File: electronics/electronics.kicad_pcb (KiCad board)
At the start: 2 copper layers, 155.2 x 120 mm, 69 parts, among them J1 GND NetTie, J2 Conn_01x02, J3 Conn 12V Out 5ch, J4 Chargers_Conn, J5 12V_BusBar, J6 GND_Busbar, J7 Conn_01x02, J9 water_sensor_conn, U1 AZ1117-ADJ, U10 BTS7006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

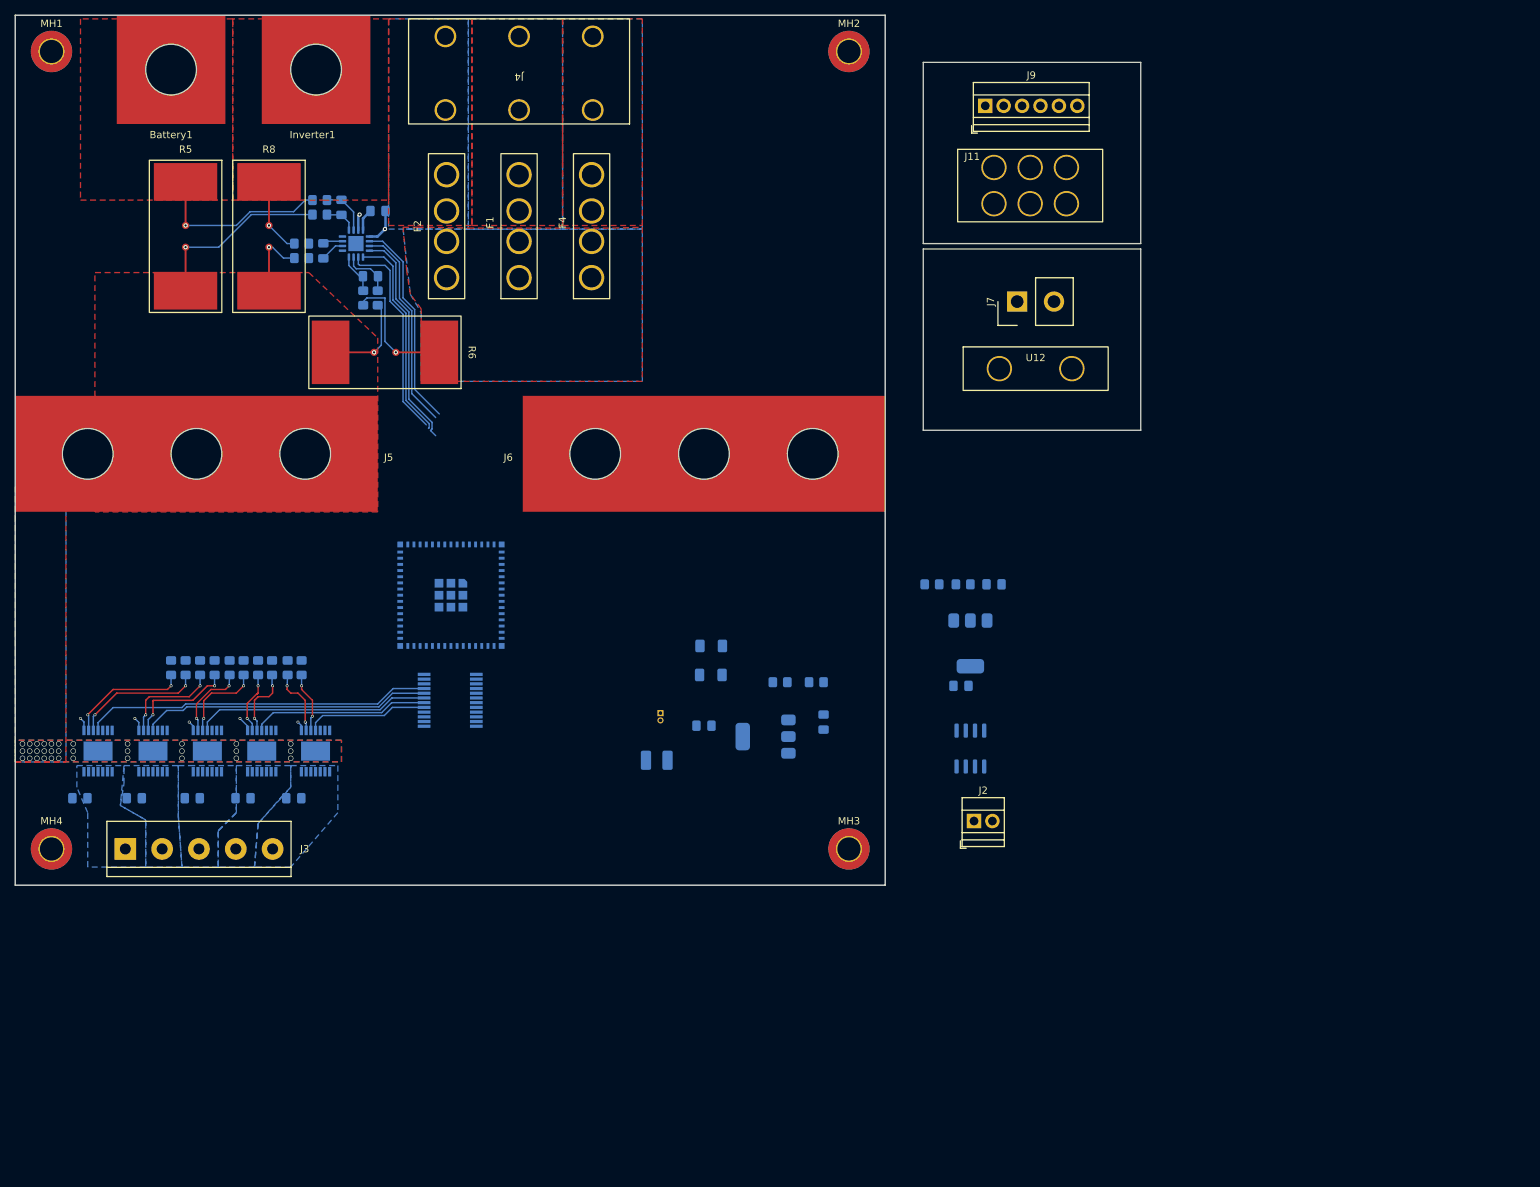
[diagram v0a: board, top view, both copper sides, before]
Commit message: big-55A-switch added
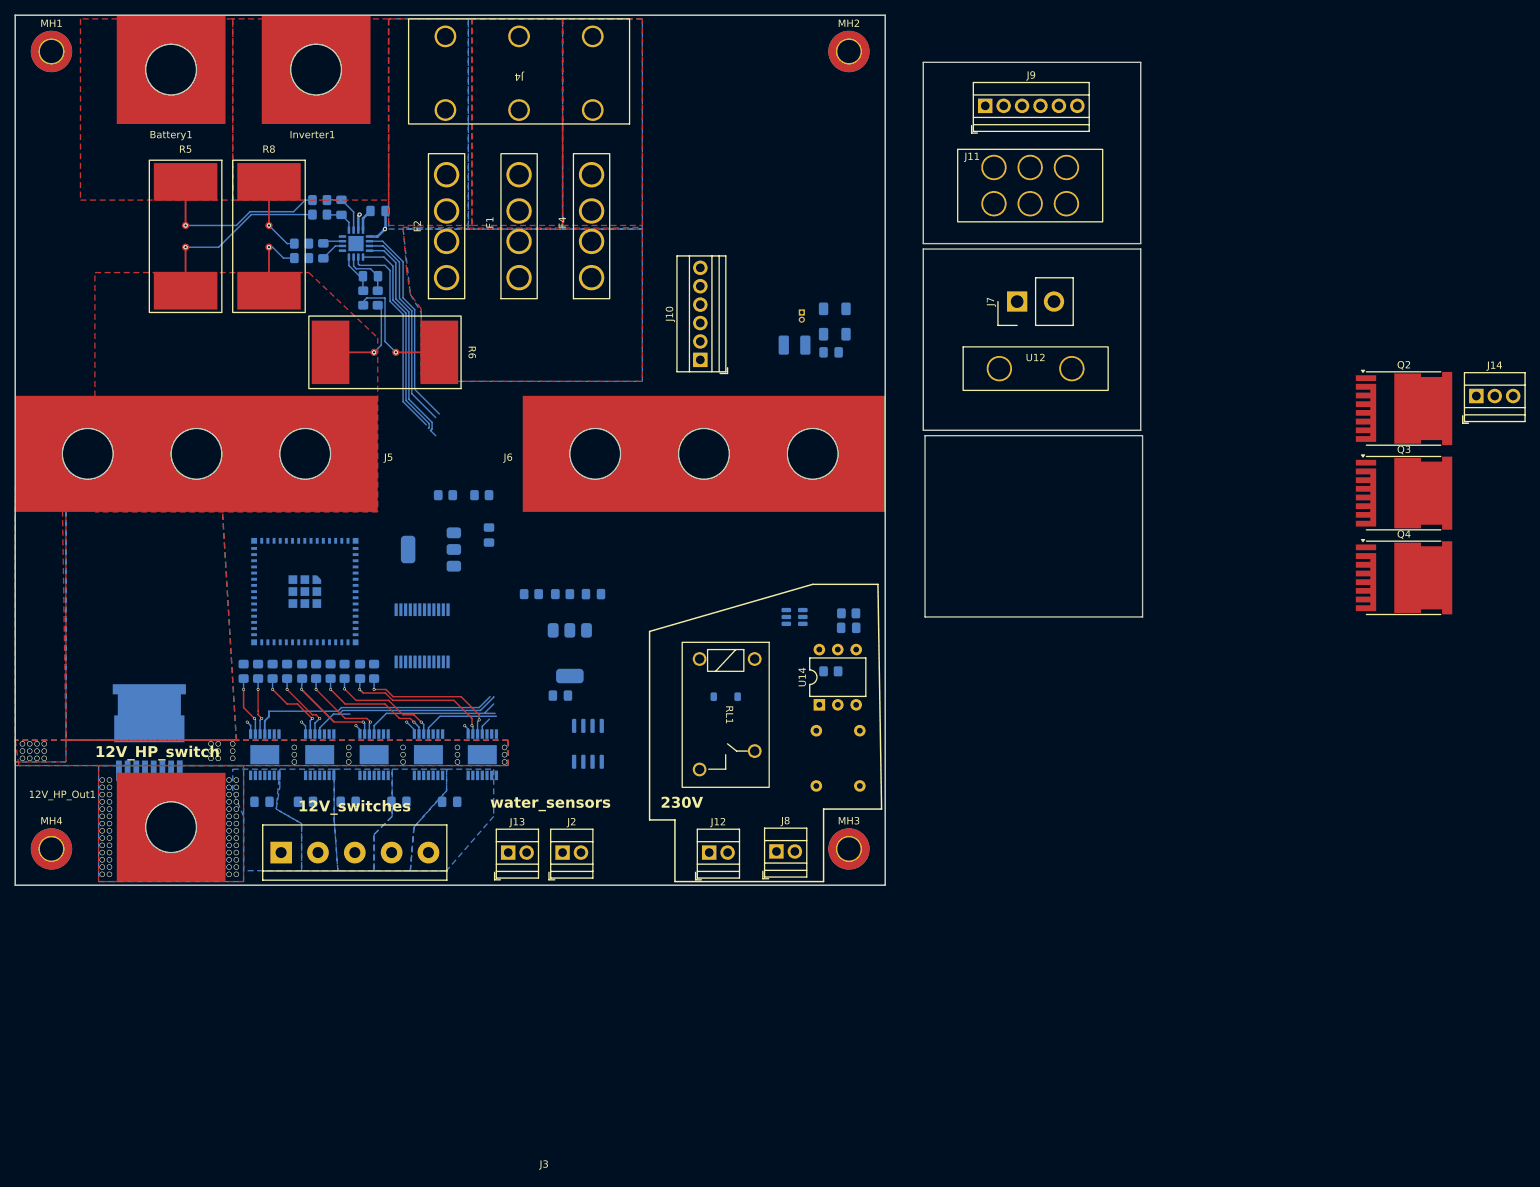
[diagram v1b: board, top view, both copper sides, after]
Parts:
- added 12V_HP_Out1: ~, HeavyDuty:high_current_pad, F.Cu at (41.5, 132.0)
- added C9: 4.7uF, Capacitor_SMD:C_0805_2012Metric_Pad1.18x1.45mm_HandSolder, B.Cu at (135.0, 104.5)
- added D2: 1N4148W, Diode_SMD:D_SOD-123, B.Cu at (118.0, 114.0)
- added J10: water_sensor_conn, TerminalBlock:TerminalBlock_Xinya_XY308-2.54-6P_1x06_P2.54mm_Horizontal, F.Cu at (114.5, 67.5)
- added J12: Conn_01x02, TerminalBlock:TerminalBlock_Xinya_XY308-2.54-2P_1x02_P2.54mm_Horizontal, F.Cu at (115.7, 135.5)
- added J13: grey_water_sensor, TerminalBlock:TerminalBlock_Xinya_XY308-2.54-2P_1x02_P2.54mm_Horizontal, F.Cu at (88.0, 135.5)
- added J14: Conn_01x03, TerminalBlock:TerminalBlock_Xinya_XY308-2.54-3P_1x03_P2.54mm_Horizontal, F.Cu at (221.5, 72.5)
- added J8: Conn_01x02, TerminalBlock:TerminalBlock_Xinya_XY308-2.54-2P_1x02_P2.54mm_Horizontal, F.Cu at (125.0, 135.3)
- added Q2: IRF6802SD, Package_TO_SOT_SMD:Infineon_PG-HSOF-8-1, F.Cu at (211.6, 74.2)
- added Q3: IRF6802SD, Package_TO_SOT_SMD:Infineon_PG-HSOF-8-1, F.Cu at (211.6, 85.9)
- added Q4: IRF6802SD, Package_TO_SOT_SMD:Infineon_PG-HSOF-8-1, F.Cu at (211.6, 97.6)
- added R17: 100k, Resistor_THT:R_Axial_DIN0207_L6.3mm_D2.5mm_P7.62mm_Horizontal, B.Cu at (130.5, 126.3)
- added R18: 100k, Resistor_THT:R_Axial_DIN0207_L6.3mm_D2.5mm_P7.62mm_Horizontal, B.Cu at (136.5, 126.3)
- added R19: 4.7kΩ, Resistor_SMD:R_0805_2012Metric_Pad1.20x1.40mm_HandSolder, B.Cu at (132.5, 110.5)
- added R20: 50 Ohm, Resistor_SMD:R_0805_2012Metric_Pad1.20x1.40mm_HandSolder, B.Cu at (135.0, 102.5)
- added RL1: AZSR131-1AE-12D, HeavyDuty:PRE29-same-sky, F.Cu at (119.0, 116.5)
- added U13: BTS50010, HeavyDuty:PG-HSOF-8, B.Cu at (38.0, 119.0)
- added U14: H11AA1, Package_DIP:DIP-6_W7.62mm, F.Cu at (130.9, 115.1)
- added U15: CNY17-1, Package_TO_SOT_SMD:SOT-23-6, B.Cu at (127.5, 103.0)
- J2: value Conn_01x02 -> CAN
- U4: footprint RF_Module:ESP32-S2-MINI-1U -> PCM_Espressif:ESP32-S2-MINI-1U
- moved D1 60.3 mm to (127.5, 65.5)
- moved J1 58.6 mm to (128.5, 61.0)
- moved J2 56.9 mm to (95.5, 135.5)
- moved R3 55.3 mm to (95.5, 99.8)
- moved U2 55.3 mm to (96.5, 108.0)
- moved C1 55.3 mm to (99.8, 99.8)
- moved C4 55.3 mm to (95.2, 113.8)
- moved R4 55.3 mm to (91.2, 99.8)
- moved C3 54.4 mm to (132.5, 66.5)
- moved C2 52.9 mm to (85.3, 91.7)
- moved R1 52.9 mm to (84.3, 86.2)
- moved R2 52.9 mm to (79.3, 86.2)
- moved U1 52.9 mm to (77.3, 93.7)
- moved U3 52.8 mm to (99.0, 120.5)
- moved R15 50.0 mm to (133.1, 64.0)
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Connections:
- J11 pad 1: Net-(J11-COM) -> /water_sensor/COM
- J7 pad 1: Net-(J7-Pin_1) -> /water_sensor/COM
- J7 pad 2: Net-(J7-Pin_2) -> unconnected-(J7-Pin_2-Pad2)
- J9 pad 1: Net-(J11-COM) -> /water_sensor/COM
- U12 pad 1: Net-(J7-Pin_1) -> unconnected-(U12-COM-Pad1)
- U12 pad 2: Net-(J7-Pin_2) -> unconnected-(U12-LVL_0-Pad2)
- U4 pad 15: unconnected-(U4-IO11-Pad15) -> /central_control_unit/water_sens_enable
- U4 pad 26: unconnected-(U4-IO26-Pad26) -> /central_control_unit/LED_B
- U4 pad 28: unconnected-(U4-IO33-Pad28) -> /central_control_unit/LED_G
- U4 pad 29: unconnected-(U4-IO34-Pad29) -> /central_control_unit/LED_R
- U4 pad 5: unconnected-(U4-IO1-Pad5) -> /central_control_unit/LED_R
- U4 pad 6: unconnected-(U4-IO2-Pad6) -> /central_control_unit/LED_G
- U4 pad 7: unconnected-(U4-IO3-Pad7) -> /central_control_unit/LED_B
- U4 pad 8: unconnected-(U4-IO4-Pad8) -> /central_control_unit/AC_DETECT
- U4 pad 9: unconnected-(U4-IO5-Pad9) -> /central_control_unit/RELAY_IN
- U5 pad 16: unconnected-(U5-I15-Pad16) -> /central_control_unit/ws_lvl_5
- U5 pad 17: unconnected-(U5-I14-Pad17) -> /central_control_unit/ws_lvl_4
- U5 pad 18: unconnected-(U5-I13-Pad18) -> /central_control_unit/ws_lvl_3
- U5 pad 19: unconnected-(U5-I12-Pad19) -> /central_control_unit/ws_lvl_2
- U5 pad 20: unconnected-(U5-I11-Pad20) -> /central_control_unit/ws_lvl_1
- U5 pad 21: unconnected-(U5-I10-Pad21) -> /central_control_unit/grey_water_tank_full
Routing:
- net /central_control_unit/CH5_DIAG: track 16.9 -> 2.46 mm
- net /central_control_unit/CH4_DIAG: track 24.5 -> 10.9 mm
- net /central_control_unit/CH1_DIAG: track 48.0 -> 34.7 mm
- net /central_control_unit/CH3_DIAG: track 32.4 -> 20.4 mm
- net Net-(U10-IN): track 9.40 -> 21.4 mm
- net /central_control_unit/CH2_DIAG: track 40.0 -> 28.2 mm
- net Net-(U10-DEN): track 8.36 -> 20.2 mm
- net Net-(U6-DEN): track 17.9 -> 7.95 mm
- net Net-(U6-IN): track 16.9 -> 8.32 mm
- net Net-(U9-IN): track 8.60 -> 16.8 mm
- net Net-(U9-DEN): track 9.74 -> 15.7 mm
- net Net-(U7-DEN): track 15.2 -> 10.1 mm
- net Net-(U7-IN): track 14.1 -> 10.9 mm
- net Net-(U8-IN): track 10.8 -> 13.6 mm
- net Net-(U8-DEN): track 12.0 -> 12.6 mm
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- added copper zone on B.Cu, net Net-(12V_HP_Out1-Pad1)
- added copper zone on F.Cu, net Net-(12V_HP_Out1-Pad1)
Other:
- board size 155.2 x 120 mm -> 155.5 x 120 mm
- board text added: "!! 230V !!"
- board text added: "12V_HP_switch"
- board text added: "12V_switches"
- board text added: "230V"
- board text added: "water_sensors"

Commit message: LED RGB and temp sensor added
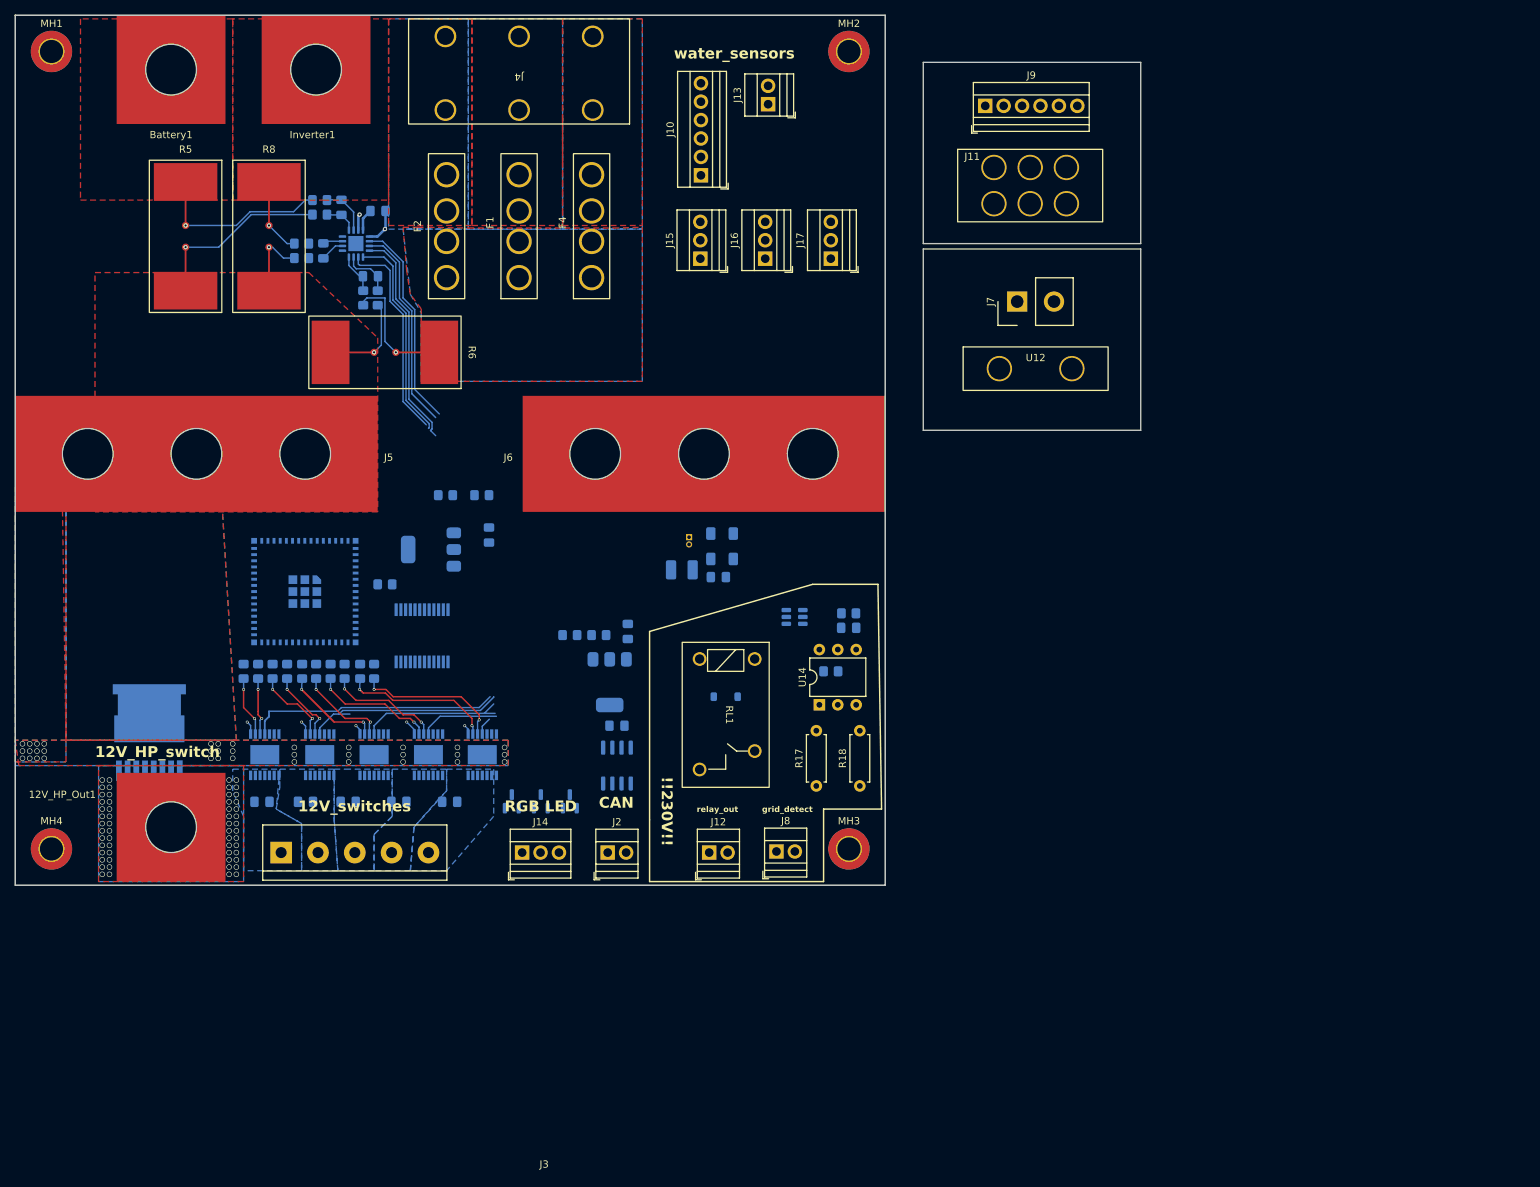
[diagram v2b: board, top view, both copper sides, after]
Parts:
- added J15: Conn_01x03, TerminalBlock:TerminalBlock_Xinya_XY308-2.54-3P_1x03_P2.54mm_Horizontal, F.Cu at (114.5, 53.6)
- added J16: Conn_01x03, TerminalBlock:TerminalBlock_Xinya_XY308-2.54-3P_1x03_P2.54mm_Horizontal, F.Cu at (123.5, 53.6)
- added J17: Conn_01x03, TerminalBlock:TerminalBlock_Xinya_XY308-2.54-3P_1x03_P2.54mm_Horizontal, F.Cu at (132.5, 53.6)
- added R21: 4.7k, Resistor_SMD:R_0805_2012Metric_Pad1.20x1.40mm_HandSolder, B.Cu at (71.0, 98.5)
- Q2, Q3, Q4: value IRF6802SD -> DMN2040U; footprint Package_TO_SOT_SMD:Infineon_PG-HSOF-8-1 -> Package_TO_SOT_SMD:SOT-23; moved to B.Cu
- R17, R18: moved to F.Cu
- moved J14 145.9 mm to (89.9, 135.5)
- moved Q2 130.8 mm to (92.5, 128.4), turned to 90 degrees
- moved Q4 126.9 mm to (88.5, 128.4), turned to 90 degrees
- moved Q3 122.7 mm to (96.5, 128.4), turned to 90 degrees
- moved J13 109.3 mm to (123.8, 32.3), turned to 90 degrees
- moved R14 34.7 mm to (117.5, 91.5)
- moved R15 34.7 mm to (117.5, 95.0)
- moved C3 34.7 mm to (117.0, 97.5)
- moved D1 34.7 mm to (112.0, 96.5)
- moved J1 34.7 mm to (113.0, 92.0)
- moved J10 25.5 mm to (114.6, 42.1)
- moved C4 8.84 mm to (103.0, 118.0)
- moved R4 7.75 mm to (96.5, 105.5)
- moved R3 7.54 mm to (100.5, 105.5)
- moved C1 7.00 mm to (104.5, 105.0), turned to -90 degrees
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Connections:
- Q2 pad 1: /central_control_unit/LED_control/V_Bat -> /central_control_unit/LED_G
- Q2 pad 2: /central_control_unit/LED_R -> Net-(J14-Pin_2)
- Q2 pad 3: Net-(J14-Pin_1) -> /central_control_unit/LED_control/V_Bat
- Q3 pad 1: /central_control_unit/LED_control/V_Bat -> /central_control_unit/LED_B
- Q3 pad 2: /central_control_unit/LED_G -> Net-(J14-Pin_3)
- Q3 pad 3: Net-(J14-Pin_2) -> /central_control_unit/LED_control/V_Bat
- Q4 pad 1: /central_control_unit/LED_control/V_Bat -> /central_control_unit/LED_R
- Q4 pad 2: /central_control_unit/LED_B -> Net-(J14-Pin_1)
- Q4 pad 3: Net-(J14-Pin_3) -> /central_control_unit/LED_control/V_Bat
- U4 pad 25: unconnected-(U4-IO21-Pad25) -> /central_control_unit/temp_sensors/1-WIRE
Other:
- board size 155.5 x 120 mm -> 155.2 x 120 mm
- board text added: "!!230V!!"
- board text added: "CAN"
- board text added: "RGB LED"
- board text added: "grid_detect"
- board text added: "relay_out"
- board text removed: "230V"
